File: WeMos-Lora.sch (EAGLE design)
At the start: 25 parts, among them P1 PADNORMAL, P2 PADNORMAL, P3 PADNORMAL, P4 PADNORMAL, U1 24AA02E64T

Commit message: * Removed LEDs + Switch * Freed GPIO16
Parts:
- removed BTN: DHT-4235A, Switch-2016:SMD-BUTTON-TOP-DHT-4235A(4P-4.2X3.2MM)
- removed C3, C4: 100nF, _c2h:CAP0805-CAP
- removed D1: 1N4148, Seeed-Discrete:D-ESD-2P-CESD5V0D1
- removed JP4: JUMPER-PAD-2-NC_BY_TRACE, SparkFun-Passives:JUMPER-PAD-2-NC_BY_TRACE
- removed P1, P2, P3, P4: PADNORMAL, _c2h:PADNORMAL
- removed WS1, WS2812: WS2812B, _c2h:WS2812BSMD
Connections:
- removed net DO: P2.1, WS1.DOUT
- removed net N$1: WS1.DIN, WS2812.DOUT
- removed net VLED: C3.1, D1.2, JP4.1, WS2812.VDD
- net 3V3: no longer P4.1
- net 5V: no longer C4.1, D1.1, JP4.2, P1.1, WS1.VDD
- net GND: no longer BTN.B0, C3.2, C4.2, P3.1, WS1.GND, WS2812.GND
- net GPIO0: no longer WS2812.DIN
- net GPIO16: no longer U$5.SEL
- net GPIO2: now also U$5.SEL; no longer BTN.A0
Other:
- note removed: "FLASH/RGBLED"
- note removed: "Switch"
- note removed: "WeMos already has a pullup on GPIO2"

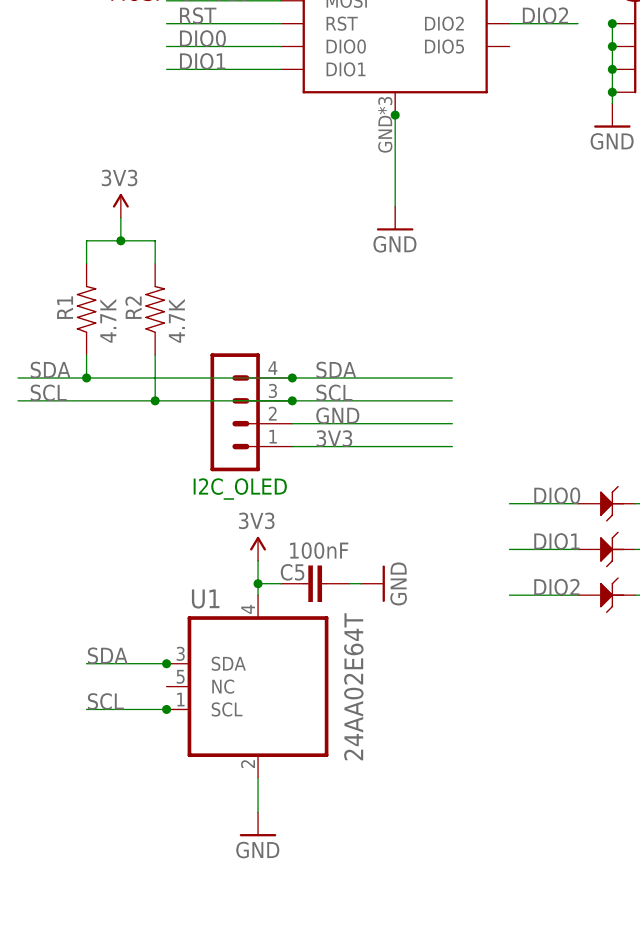
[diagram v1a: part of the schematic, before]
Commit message: Removed display connector
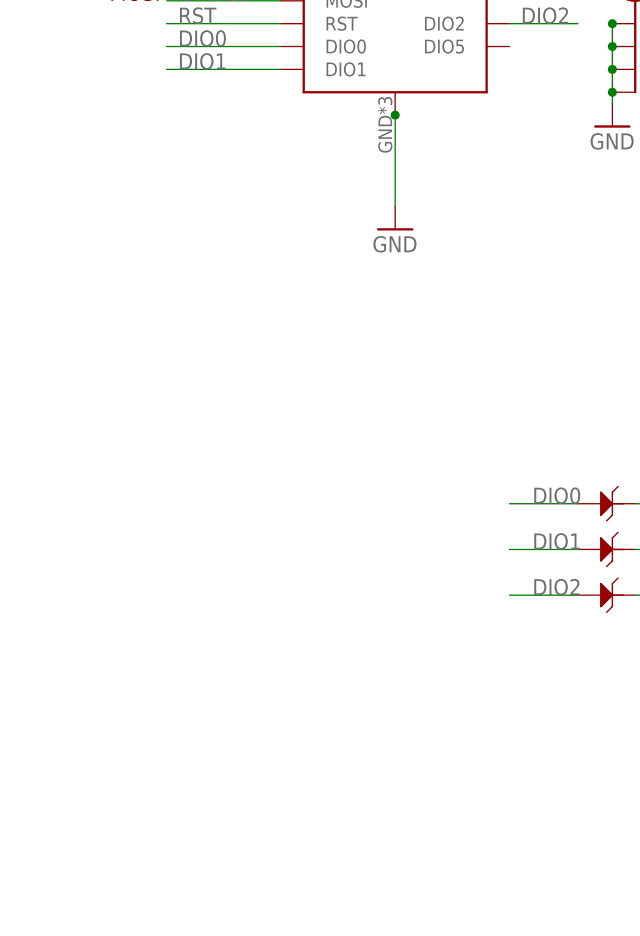
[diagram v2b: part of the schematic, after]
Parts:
- removed C5: 100nF, _c2h:CAP0805-CAP
- removed I2C_OLED: CON_HEADER_1X04'LOCK', _c2h:CON_HEADER_1X04'LOCK'
- removed R1, R2: 4.7K, _c2h:RESISTOR0805-RES
- removed U1: 24AA02E64T, Microchip-24AA02E64T:24AA02E64T-I/OT
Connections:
- net 3V3: no longer C5.1, I2C_OLED.1, R1.2, R2.2, U1.VCC
- net GND: no longer C5.2, I2C_OLED.2, U1.VSS
- net SCL: no longer I2C_OLED.3, R2.1, U1.SCL
- net SDA: no longer I2C_OLED.4, R1.1, U1.SDA
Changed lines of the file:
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@@
 <layer number="59" name="tCarbon" color="7" fill="1" visible="no" active="no"/>
 <layer number="60" name="bCarbon" color="7" fill="1" visible="no" active="no"/>
-<layer number="90" name="Modules" color="5" fill="1" visible="no" active="yes"/>
+<layer number="90" name="Modules" color="5" fill="1" visible="yes" active="yes"/>
 <layer number="91" name="Nets" color="2" fill="1" visible="yes" active="yes"/>
 <layer number="92" name="Busses" color="1" fill="1" visible="yes" active="yes"/>
@@
 </classes>
 <parts>
-<part name="R1" library="_c2h" deviceset="RESISTOR" device="0805-RES" value="4.7K"/>
-<part name="R2" library="_c2h" deviceset="RESISTOR" device="0805-RES" value="4.7K"/>
-<part name="I2C_OLED" library="_c2h" deviceset="CON_HEADER_1X04" device="'LOCK'" value="CON_HEADER_1X04'LOCK'"/>
 <part name="NAME" library="SparkFun-Aesthetics" deviceset="FRAME-A4L" device="" value="Value">
-<attribute name="CNAME" value="ESP8266 WeMos Lora Shield"/>
-<attribute name="CREVISION" value="1.1"/>
-<attribute name="DESIGNER" value="Charles-Henri Hallard"/>
+<attribute name="CNAME" value="ESP8266 WeMos Lora Micro"/>
+<attribute name="CREVISION" value="1.0"/>
+<attribute name="DESIGNER" value="C. Hallard + C. Näveke"/>
 </part>
-<part name="P+7" library="_c2h" deviceset="3V3-EXT" device="" value="3V3"/>
 <part name="JP2" library="SparkFun-Connectors" deviceset="M08" device="NO_SILK_FEMALE_PTH"/>
 <part name="JP1" library="SparkFun-Connectors" deviceset="M08" device="NO_SILK_FEMALE_PTH"/>
@@
 <part name="D3" library="Seeed-Discrete" deviceset="D-ESD-2P" device="-CESD5V0D1" value="1N4148"/>
 <part name="D4" library="Seeed-Discrete" deviceset="D-ESD-2P" device="-CESD5V0D1" value="1N4148"/>
-<part name="U1" library="Microchip-24AA02E64T" deviceset="24AA02E64T-I/OT" device="" value="24AA02E64T"/>
-<part name="P+3" library="_c2h" deviceset="3V3-EXT" device="" value="3V3"/>
-<part name="GND8" library="supply1" deviceset="GND" device=""/>
 <part name="J$2" library="_c2h" deviceset="ANTENNA" device="TINY"/>
-<part name="C5" library="_c2h" deviceset="CAP" device="0805-CAP" value="100nF"/>
-<part name="GND7" library="SparkFun" deviceset="GND" device=""/>
 </parts>
 <sheets>
@@
 </plain>
 <instances>
-<instance part="R1" gate="G$1" x="41.91" y="82.55" smashed="yes" rot="R90">
-<attribute name="NAME" x="40.4114" y="81.28" size="1.778" layer="95" rot="R90"/>
-<attribute name="VALUE" x="45.212" y="78.74" size="1.778" layer="96" rot="R90"/>
-</instance>
-<instance part="R2" gate="G$1" x="49.53" y="82.55" smashed="yes" rot="R90">
-<attribute name="NAME" x="48.0314" y="81.28" size="1.778" layer="95" rot="R90"/>
-<attribute name="VALUE" x="52.832" y="78.74" size="1.778" layer="96" rot="R90"/>
-</instance>
-<instance part="I2C_OLED" gate="G$1" x="54.61" y="64.77" smashed="yes">
-<attribute name="NAME" x="53.594" y="61.976" size="1.778" layer="91"/>
-</instance>
 <instance part="NAME" gate="G$1" x="5.08" y="5.08" smashed="yes">
 <attribute name="DRAWING_NAME" x="196.85" y="16.51" size="2.54" layer="94" font="vector"/>
@@
 <attribute name="CNAME" x="186.69" y="21.59" size="2.54" layer="94" font="vector"/>
 <attribute name="CREVISION" x="240" y="6.25" size="2.54" layer="94" font="vector"/>
-</instance>
-<instance part="P+7" gate="3V3-EXT" x="45.72" y="92.71" smashed="yes">
-<attribute name="VALUE" x="43.434" y="96.266" size="1.778" layer="96"/>
 </instance>
 <instance part="JP2" gate="G$1" x="153.67" y="133.35" rot="R180"/>
@@
 <instance part="D3" gate="G$1" x="100.33" y="55.88" smashed="yes"/>
 <instance part="D4" gate="G$1" x="100.33" y="50.8" smashed="yes"/>
-<instance part="U1" gate="A" x="63.5" y="43.18" smashed="yes">
-<attribute name="NAME" x="53.3908" y="49.3522" size="2.0828" layer="95" ratio="10" rot="SR0"/>
-<attribute name="VALUE" x="72.644" y="32.258" size="2.0828" layer="96" ratio="10" rot="SR90"/>
-</instance>
-<instance part="P+3" gate="3V3-EXT" x="60.96" y="54.61" smashed="yes">
-<attribute name="VALUE" x="58.674" y="58.166" size="1.778" layer="96"/>
-</instance>
-<instance part="GND8" gate="1" x="60.96" y="24.13"/>
 <instance part="J$2" gate="1" x="102.87" y="119.38"/>
-<instance part="C5" gate="G$1" x="68.58" y="52.07" smashed="yes" rot="R90">
-<attribute name="NAME" x="66.294" y="54.229" size="1.778" layer="95" rot="R180"/>
-<attribute name="VALUE" x="71.12" y="56.642" size="1.778" layer="96" rot="R180"/>
-</instance>
-<instance part="GND7" gate="1" x="74.93" y="52.07" smashed="yes" rot="R90">
-<attribute name="VALUE" x="77.47" y="49.53" size="1.778" layer="96" rot="R90"/>
-</instance>
 </instances>
 <busses>
@@
 <nets>
 <net name="GND" class="0">
-<segment>
-<pinref part="I2C_OLED" gate="G$1" pin="2"/>
-<label x="67.31" y="69.85" size="1.778" layer="95"/>
-<wire x1="82.55" y1="69.85" x2="64.77" y2="69.85" width="0.1524" layer="91"/>
-</segment>
 <segment>
 <pinref part="GND9" gate="1" pin="GND"/>
@@
 </segment>
 <segment>
-<pinref part="U1" gate="A" pin="VSS"/>
-<pinref part="GND8" gate="1" pin="GND"/>
-<wire x1="60.96" y1="26.67" x2="60.96" y2="30.48" width="0.1524" layer="91"/>
-</segment>
-<segment>
-<pinref part="C5" gate="G$1" pin="2"/>
-<pinref part="GND7" gate="1" pin="GND"/>
-<wire x1="71.12" y1="52.07" x2="72.39" y2="52.07" width="0.1524" layer="91"/>
-</segment>
-<segment>
 <pinref part="JP1" gate="G$1" pin="7"/>
 <wire x1="184.15" y1="125.73" x2="189.23" y2="125.73" width="0.1524" layer="91"/>
@@
 <net name="SCL" class="0">
 <segment>
-<label x="35.56" y="72.39" size="1.778" layer="95"/>
-<pinref part="R2" gate="G$1" pin="1"/>
-<wire x1="64.77" y1="72.39" x2="49.53" y2="72.39" width="0.1524" layer="91"/>
-<wire x1="49.53" y1="77.47" x2="49.53" y2="72.39" width="0.1524" layer="91"/>
-<wire x1="49.53" y1="72.39" x2="34.29" y2="72.39" width="0.1524" layer="91"/>
-<junction x="49.53" y="72.39"/>
-<label x="67.31" y="72.39" size="1.778" layer="95"/>
-<pinref part="I2C_OLED" gate="G$1" pin="3"/>
-<junction x="64.77" y="72.39"/>
-<wire x1="82.55" y1="72.39" x2="64.77" y2="72.39" width="0.1524" layer="91"/>
-</segment>
-<segment>
 <pinref part="JP1" gate="G$1" pin="3"/>
 <wire x1="184.15" y1="135.89" x2="189.23" y2="135.89" width="0.1524" layer="91"/>
 <label x="184.15" y="135.89" size="1.778" layer="95"/>
 </segment>
-<segment>
-<wire x1="50.8" y1="38.1" x2="41.91" y2="38.1" width="0.1524" layer="91"/>
-<label x="41.91" y="38.1" size="1.778" layer="95"/>
-<pinref part="U1" gate="A" pin="SCL"/>
-<junction x="50.8" y="38.1"/>
-</segment>
 </net>
 <net name="SDA" class="0">
-<segment>
-<label x="35.56" y="74.93" size="1.778" layer="95"/>
-<pinref part="R1" gate="G$1" pin="1"/>
-<wire x1="64.77" y1="74.93" x2="41.91" y2="74.93" width="0.1524" layer="91"/>
-<wire x1="41.91" y1="77.47" x2="41.91" y2="74.93" width="0.1524" layer="91"/>
-<wire x1="41.91" y1="74.93" x2="34.29" y2="74.93" width="0.1524" layer="91"/>
-<junction x="41.91" y="74.93"/>
-<label x="67.31" y="74.93" size="1.778" layer="95"/>
-<pinref part="I2C_OLED" gate="G$1" pin="4"/>
-<junction x="64.77" y="74.93"/>
-<wire x1="82.55" y1="74.93" x2="64.77" y2="74.93" width="0.1524" layer="91"/>
-</segment>
 <segment>
 <wire x1="184.15" y1="133.35" x2="189.23" y2="133.35" width="0.1524" layer="91"/>
 <pinref part="JP1" gate="G$1" pin="4"/>
 <label x="184.15" y="133.35" size="1.778" layer="95"/>
-</segment>
-<segment>
-<wire x1="50.8" y1="43.18" x2="41.91" y2="43.18" width="0.1524" layer="91"/>
-<label x="41.91" y="43.18" size="1.778" layer="95"/>
-<pinref part="U1" gate="A" pin="SDA"/>
-<junction x="50.8" y="43.18"/>
 </segment>
 </net>
@@
 </net>
 <net name="3V3" class="0">
-<segment>
-<pinref part="R2" gate="G$1" pin="2"/>
-<wire x1="49.53" y1="90.17" x2="45.72" y2="90.17" width="0.1524" layer="91"/>
-<wire x1="45.72" y1="90.17" x2="41.91" y2="90.17" width="0.1524" layer="91"/>
-<wire x1="49.53" y1="87.63" x2="49.53" y2="90.17" width="0.1524" layer="91"/>
-<pinref part="R1" gate="G$1" pin="2"/>
-<wire x1="41.91" y1="87.63" x2="41.91" y2="90.17" width="0.1524" layer="91"/>
-<pinref part="P+7" gate="3V3-EXT" pin="3V3-EXT"/>
-<wire x1="45.72" y1="92.71" x2="45.72" y2="90.17" width="0.1524" layer="91"/>
-<junction x="45.72" y="90.17"/>
-</segment>
 <segment>
 <wire x1="76.2" y1="132.08" x2="76.2" y2="139.7" width="0.1524" layer="91"/>
@@
 <label x="140.97" y="123.19" size="1.778" layer="95"/>
 </segment>
-<segment>
-<pinref part="I2C_OLED" gate="G$1" pin="1"/>
-<label x="67.31" y="67.31" size="1.778" layer="95"/>
-<wire x1="82.55" y1="67.31" x2="64.77" y2="67.31" width="0.1524" layer="91"/>
-</segment>
-<segment>
-<pinref part="U1" gate="A" pin="VCC"/>
-<pinref part="P+3" gate="3V3-EXT" pin="3V3-EXT"/>
-<wire x1="60.96" y1="54.61" x2="60.96" y2="52.07" width="0.1524" layer="91"/>
-<pinref part="C5" gate="G$1" pin="1"/>
-<wire x1="60.96" y1="52.07" x2="60.96" y2="50.8" width="0.1524" layer="91"/>
-<wire x1="63.5" y1="52.07" x2="60.96" y2="52.07" width="0.1524" layer="91"/>
-<junction x="60.96" y="52.07"/>
-</segment>
-</net>
+</net>
